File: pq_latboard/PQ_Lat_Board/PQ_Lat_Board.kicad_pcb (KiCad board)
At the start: 6 copper layers, 48 x 48 mm, 27 parts, among them IC1 TCN75AVOA713, J1 Conn_01x11_MountingPin, J2 Conn_Coaxial

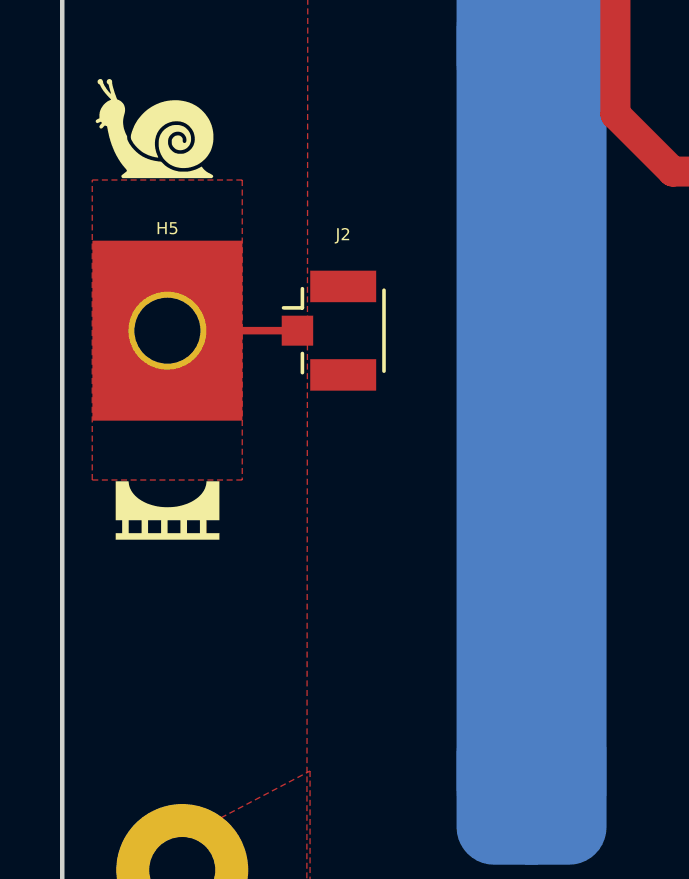
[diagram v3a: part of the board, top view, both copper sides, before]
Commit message: EPS changes in progress. Will change to a new implementation
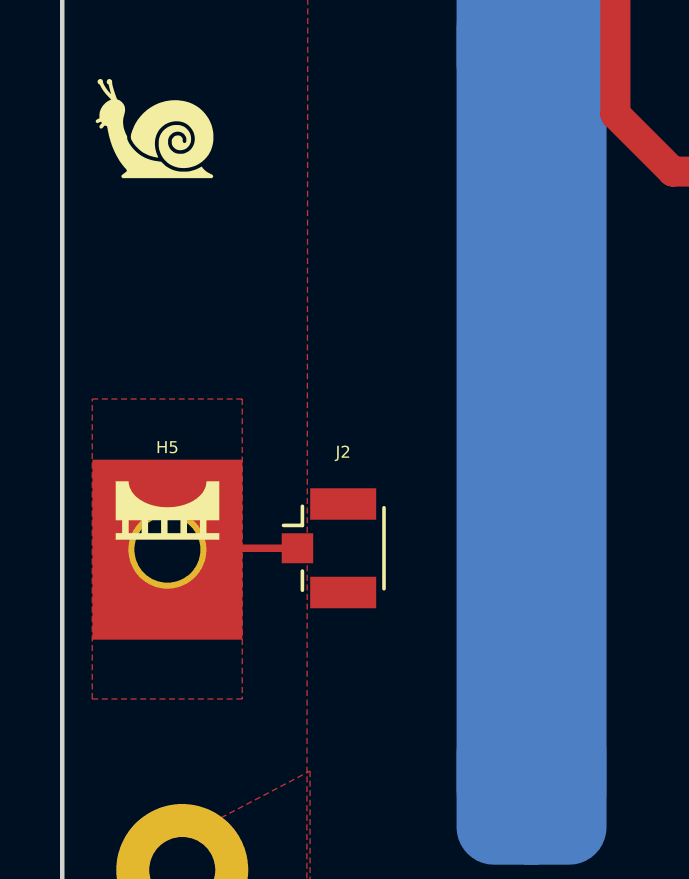
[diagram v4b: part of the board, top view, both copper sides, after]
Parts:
- moved H5 7.30 mm to (78.5, 73.3)
- moved J2 7.25 mm to (83.9, 73.3)

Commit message: lateral modification
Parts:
- removed D2: LED, LED_SMD:LED_0402_1005Metric
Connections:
- D1 pad 1: /PH- -> GND
- J1 pad 3: /VCC_MAG -> /ADCS
- J1 pad 7: /PH- -> GND
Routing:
- net /PH-: track 39.2 -> 0.00 mm, vias 1 -> 0
- net /ADCS: track 13.1 -> 15.7 mm, vias 0 -> 5
- net GND: track 0.00 -> 1.89 mm, vias 11 -> 12
- net /VCC_MAG: track 9694.4 -> 9692.7 mm, vias 5 -> 0
